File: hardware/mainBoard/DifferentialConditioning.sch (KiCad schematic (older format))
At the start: 58 parts

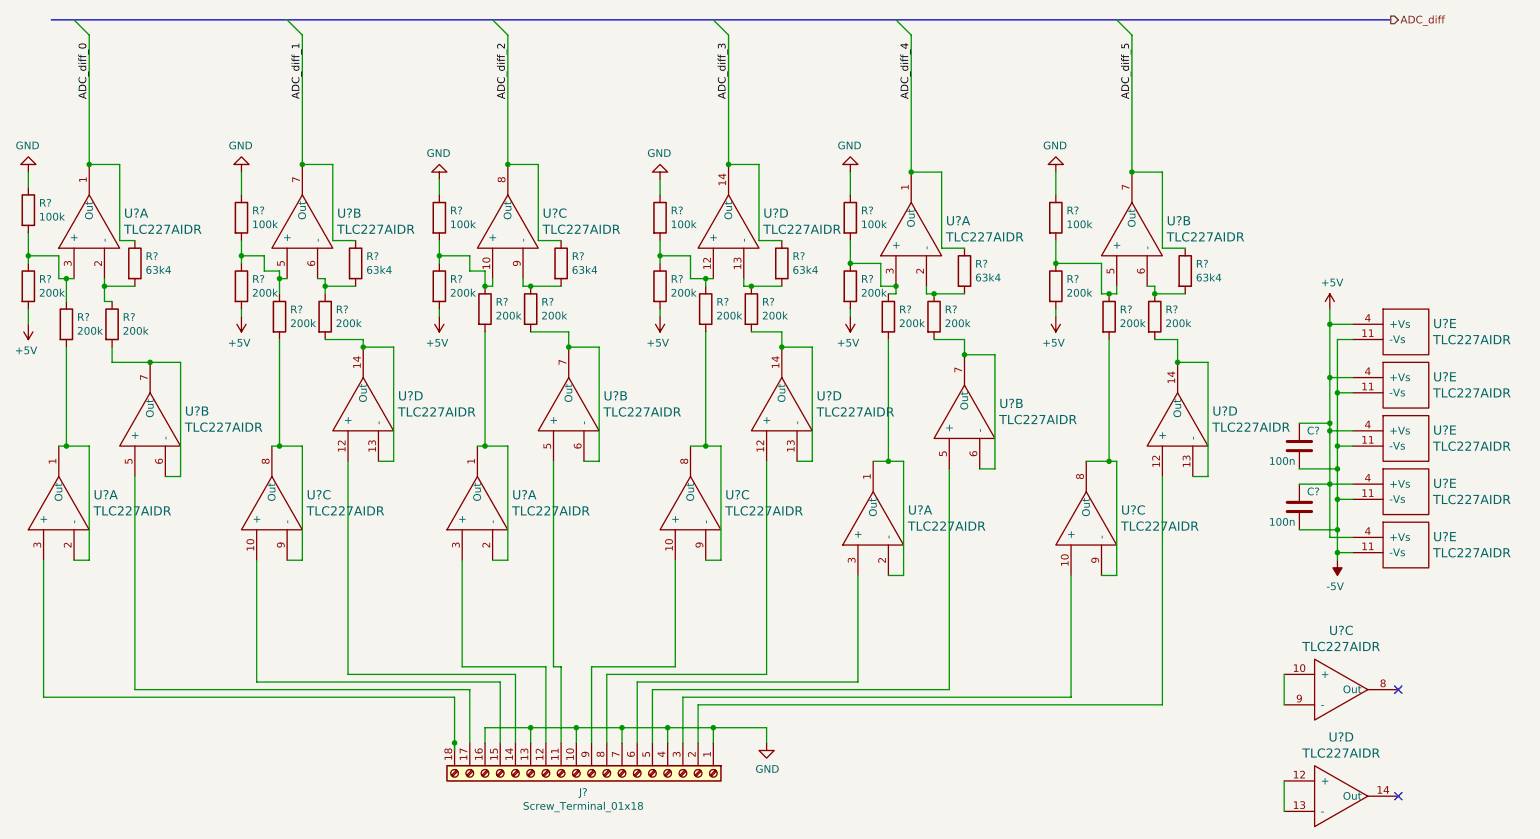
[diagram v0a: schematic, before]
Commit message: Ended schematic, created some pcb footprints
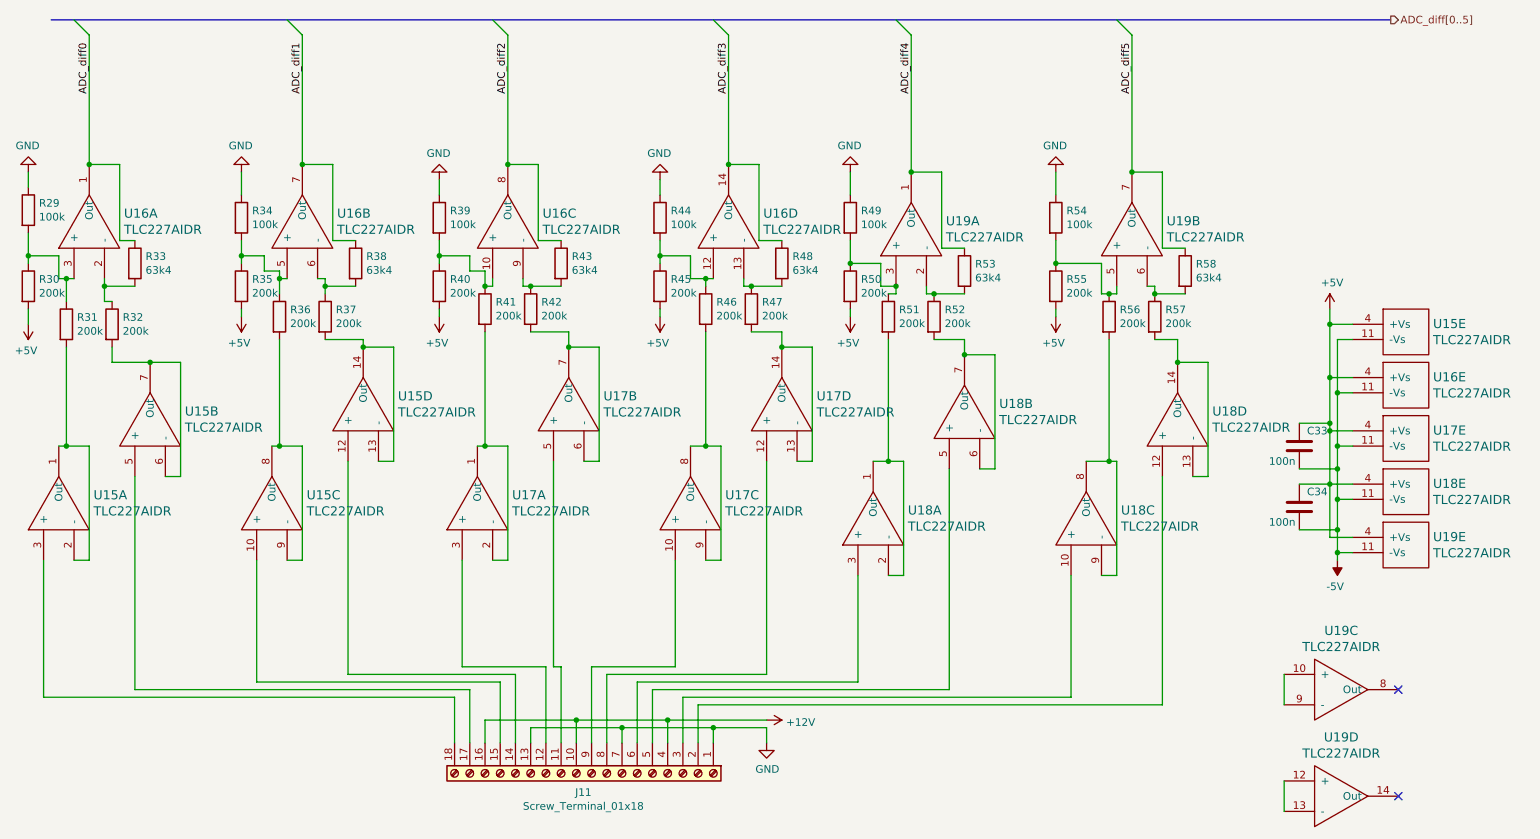
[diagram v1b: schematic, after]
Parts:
- C33, C34: renamed from C?; footprint (none) -> Capacitor_SMD:C_0603_1608Metric_Pad1.05x0.95mm_HandSolder
- J11: renamed from J?; footprint (none) -> chinalandfoot:TerminalBlock_18_P5.08mm
- R29, R30, R31, R32, R33, R34, R35, R36, R37, R38, R39, R40, R41, R42, R43, R44, R45, R46, R47, R48, R49, R50, R51, R52, R53, R54, R55, R56, R57, R58: renamed from R?; footprint (none) -> Resistor_SMD:R_0603_1608Metric_Pad1.05x0.95mm_HandSolder
- U15, U16, U17, U18, U19: renamed from U?; footprint (none) -> Package_SO:SOIC-14_3.9x8.7mm_P1.27mm
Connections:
- net GND: no longer J11.10 (Pin_10), J11.16 (Pin_16), J11.4 (Pin_4)
- net ADC_diff_0 renamed ADC_diff0
- net ADC_diff_1 renamed ADC_diff1
- net ADC_diff_2 renamed ADC_diff2
- net ADC_diff_3 renamed ADC_diff3
- net ADC_diff_4 renamed ADC_diff4
- net ADC_diff_5 renamed ADC_diff5
- new net +12V: J11.10 (Pin_10), J11.16 (Pin_16), J11.4 (Pin_4)

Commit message: First working software
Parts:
- C33, C34: URL (none) -> https://lcsc.com/product-detail/Multilayer-Ceramic-Capacito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
- R29, R30, R31, R32, R33, R34, R35, R36, R37, R38, R39, R40, R41, R42, R43, R44, R45, R46, R47, R48, R49, R50, R51, R52, R53, R54, R55, R56, R57, R58: URL (none) -> https://lcsc.com/product-detail/Chip-Resistor-Surface-Mount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
- U15, U16, U17, U18, U19: URL (none) -> https://lcsc.com/product-detail/Precision-OpAmps_Texas-Inst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
